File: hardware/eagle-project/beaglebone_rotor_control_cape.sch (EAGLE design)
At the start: 21 parts, among them IC1 TLC2264CDU, IC2 TLV5616, IC3 MAX3232ESE, Q1 SQ2348ES-T1-GE3, Q2 SQ2348ES-T1-GE3, X1 BEAGLEBONE_OUTLINE

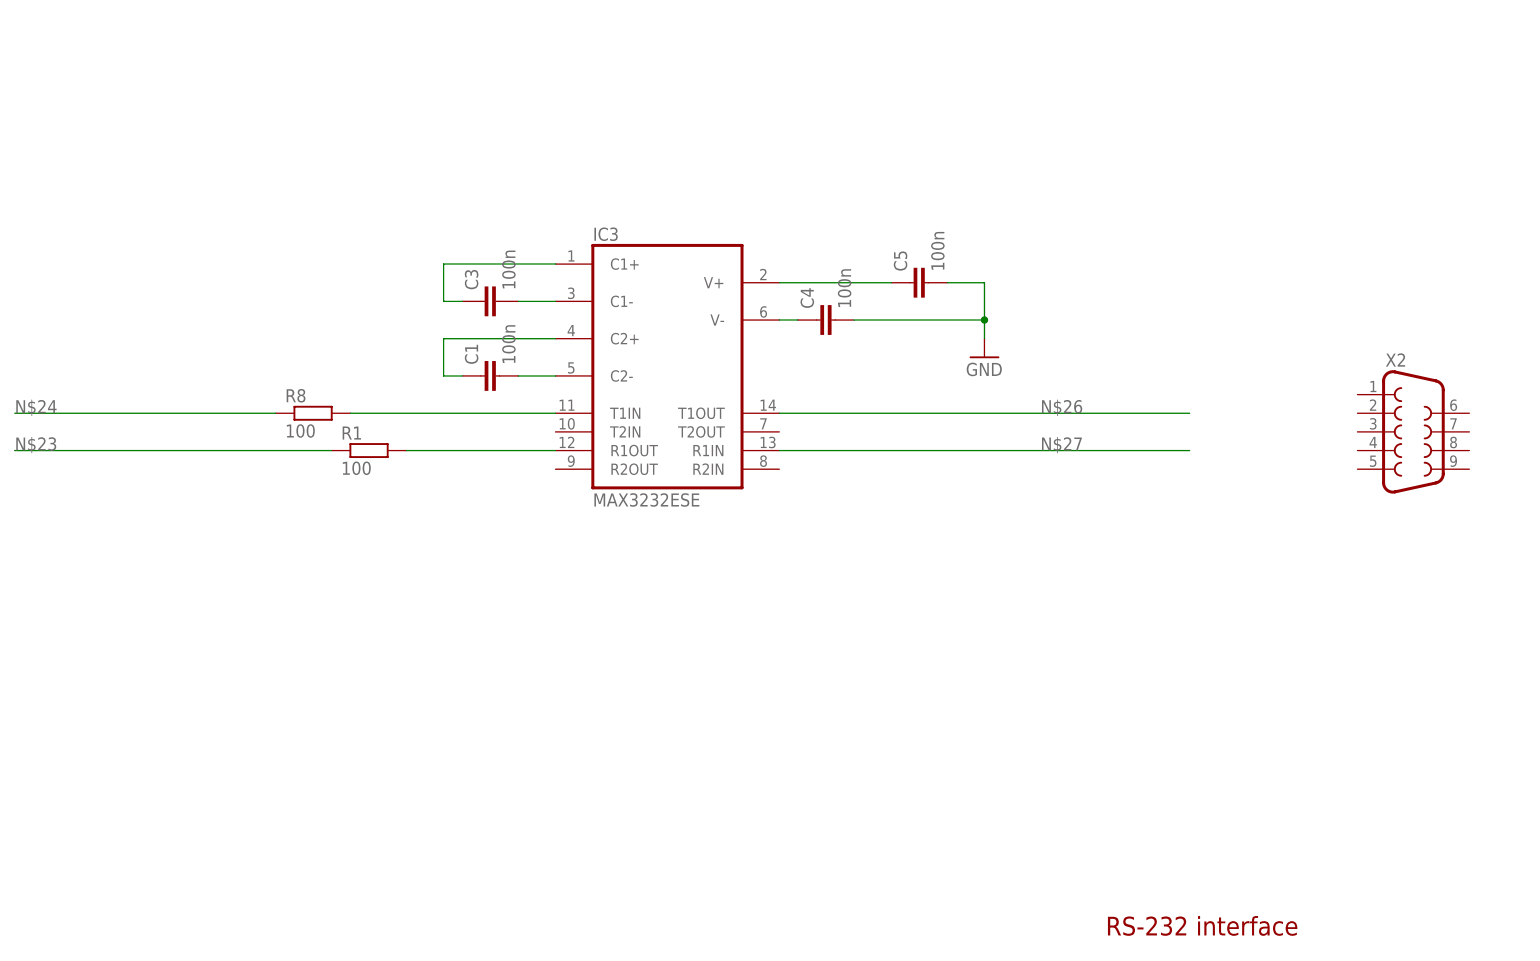
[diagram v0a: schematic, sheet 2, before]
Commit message: Eagle project update * RS232 rcv/drv layout done * AMP Press-Fit connector library created
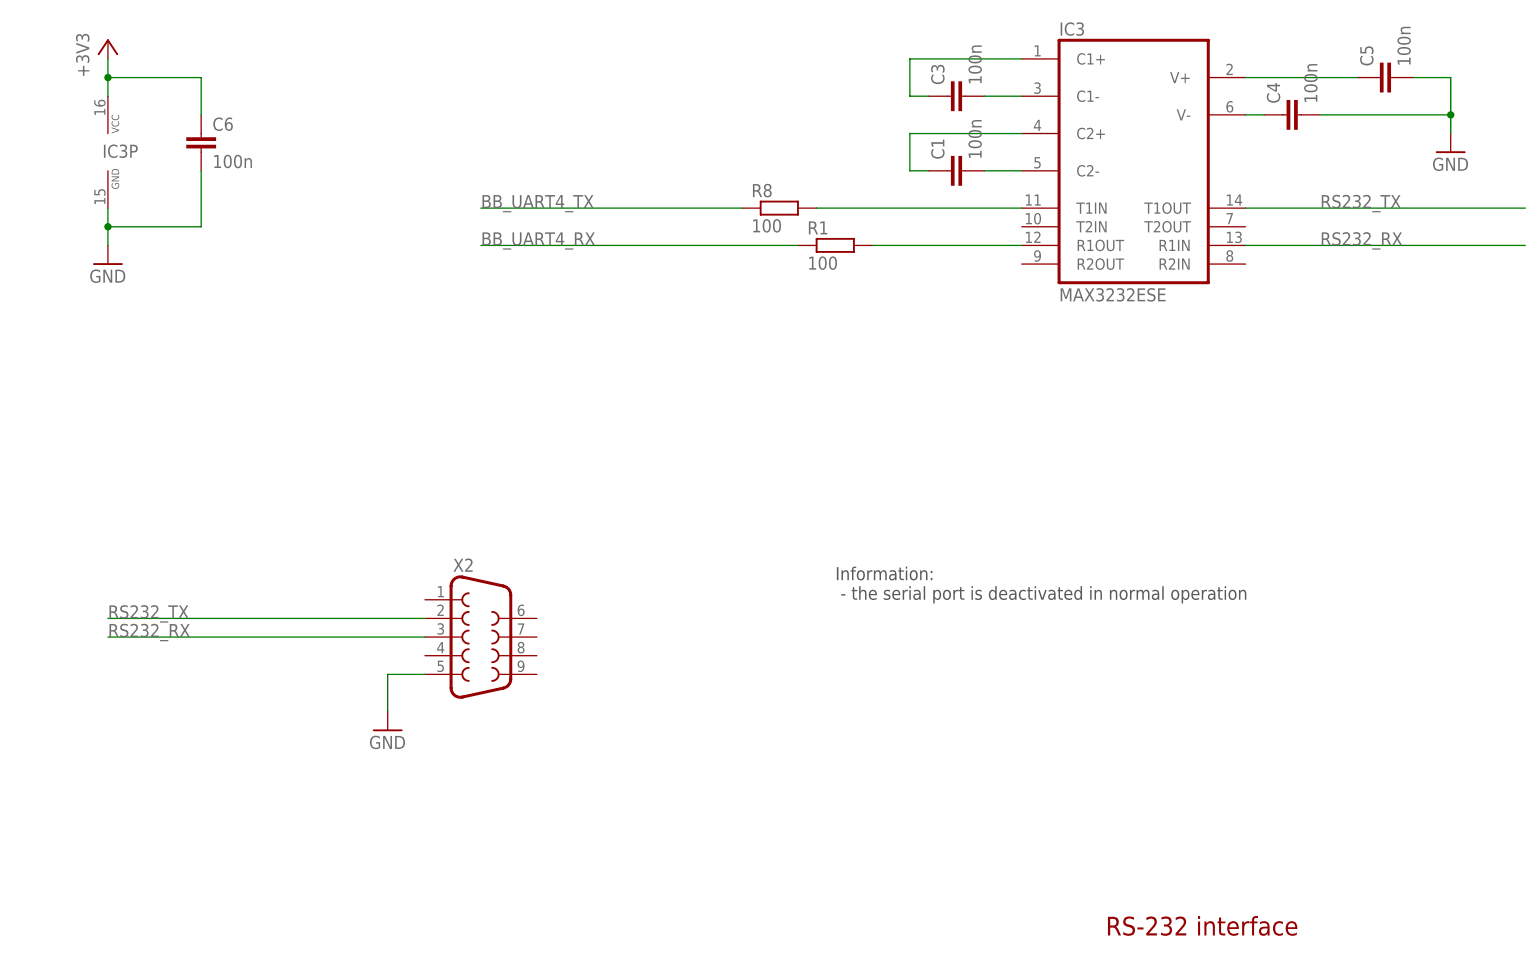
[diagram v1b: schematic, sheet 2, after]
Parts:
- removed R9: 15k, rcl:R-EU_R0805
- added C6: 100n, rcl:C-EUC0603
- added D1: BAS40-04, diode:BAS40-04
- added D2: 5V1, diode:ZENER-DIODESOT23
- added R10: 10k, rcl:R-EU_R0805
- R4: value (none) -> 10k
- R5: value (none) -> 5k6
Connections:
- removed net N$23: R1.1
- removed net N$24: R8.1
- removed net N$26: IC3G$1.T1OUT
- removed net N$27: IC3G$1.R1IN
- new net +3V3: C6.1, IC3P.VCC, X1.VDD_3V3EXP@1, X1.VDD_3V3EXP@2
- new net BB_UART4_RX: R1.1, X1.UART4_RXD
- new net BB_UART4_TX: R8.1, X1.UART4_TXD
- new net N$28: R10.2
- new net RS232_RX: IC3G$1.R1IN, X2.3
- new net RS232_TX: IC3G$1.T1OUT, X2.2
- net +5V: now also D1.C2, X1.VDD_5V@1, X1.VDD_5V@2
- net GND: now also C6.2, D1.A1, D2.A, IC3P.GND, X2.5; no longer R9.1
- net N$12: now also D1.C1A2, D2.C, R10.1; no longer R9.2
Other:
- note added: "Information: - the serial port is deactivated in normal operation"
- note removed: "todo überspannungsschutz"
- moved on the sheet: C1, C2, C3, C4, C5, IC1B, IC3, R1, R4, R5, R8, X2

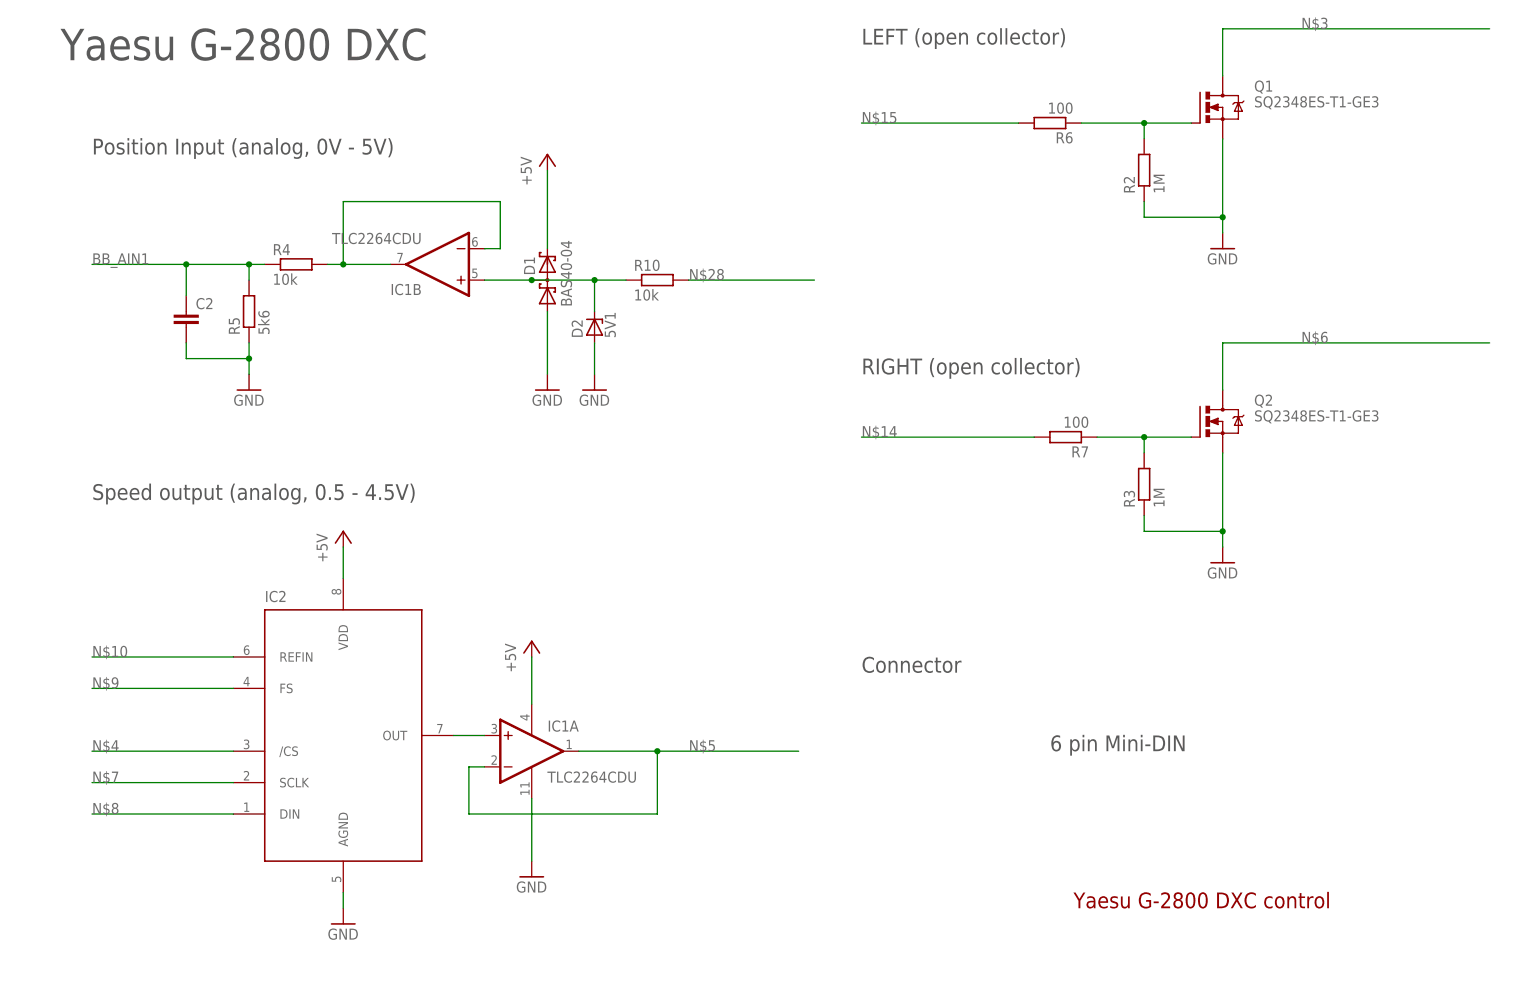
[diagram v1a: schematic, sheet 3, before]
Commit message: Updated available components list
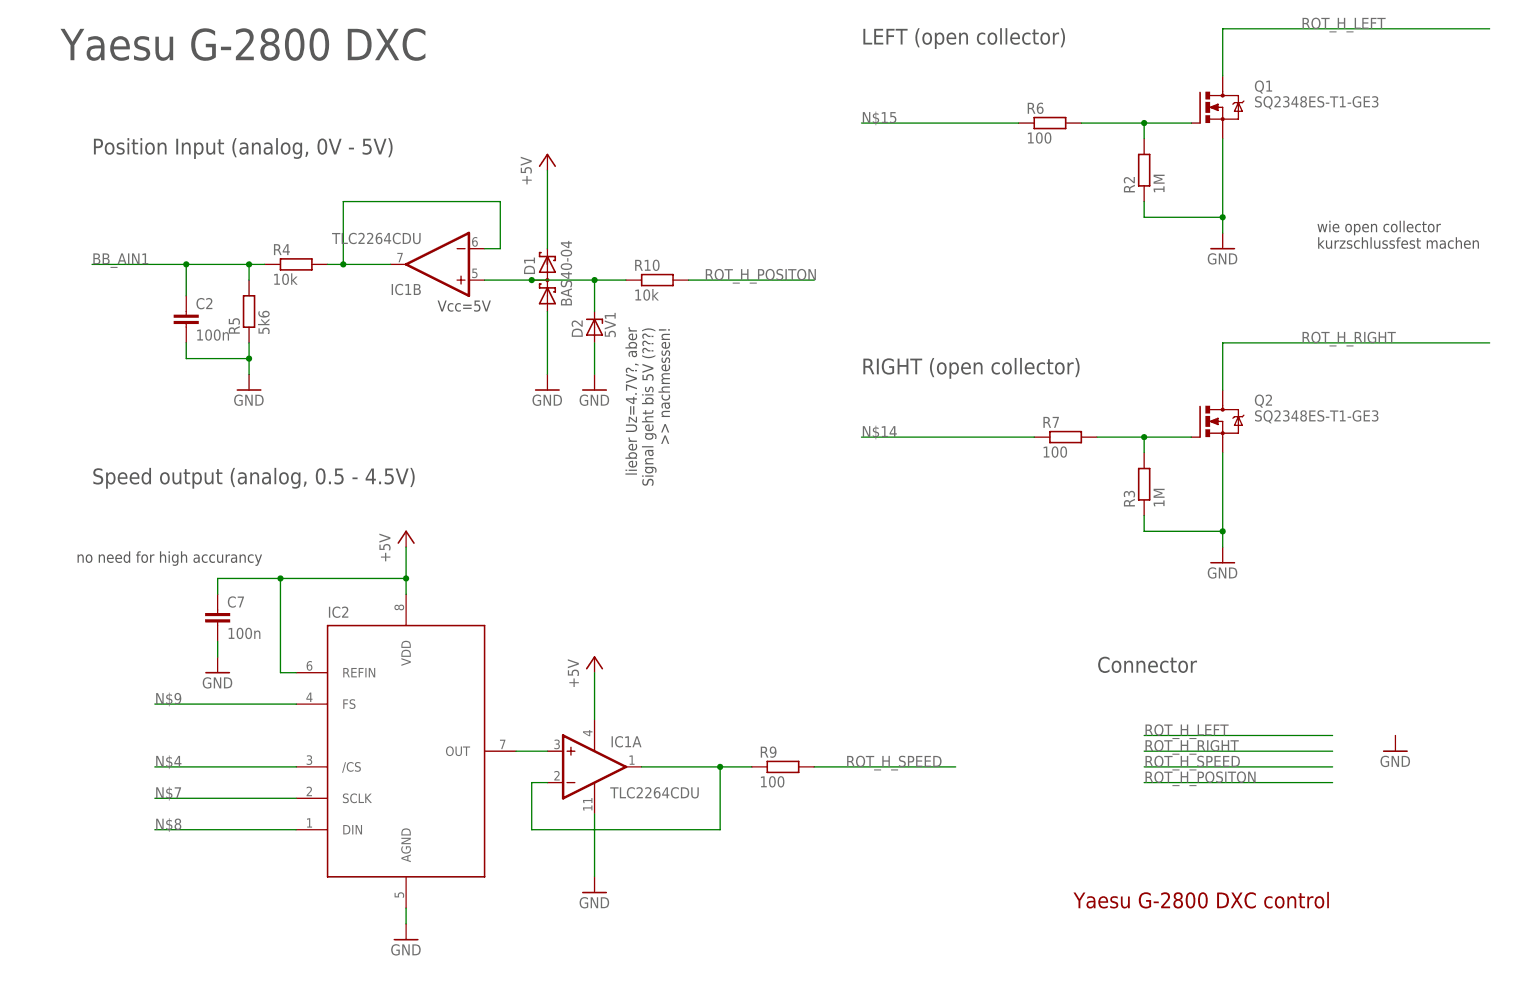
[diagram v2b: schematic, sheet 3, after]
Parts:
- added C7: 100n, rcl:C-EUC0603
- added R9: 100, rcl:R-EU_R0805
- C2: value (none) -> 100n
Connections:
- net N$28 renamed ROT_H_POSITON
- net N$3 renamed ROT_H_LEFT
- net N$6 renamed ROT_H_RIGHT
- removed net N$10: IC2.REFIN
- new net ROT_H_SPEED: R9.2
- net +5V: now also C7.1, IC2.REFIN
- net GND: now also C7.2
- net N$11: now also R7.2; no longer R7.1
- net N$13: now also R6.2; no longer R6.1
- net N$14: now also R7.1; no longer R7.2
- net N$15: now also R6.1; no longer R6.2
- net N$5: now also R9.1
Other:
- note added: "Vcc=5V"
- note added: "lieber Uz=4.7V?, aber Signal geht bis 5V (???) >> nachmessen!"
- note added: "no need for high accurancy"
- note added: "wie open collector kurzschlussfest machen"
- note removed: "6 pin Mini-DIN"
- moved on the sheet: IC1A, IC2, R6, R7

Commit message: New comments/thoughts in EAGLE schematics
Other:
- note added: "no need for high accurancy, maybe read this voltage for reference with ADC?"
- note removed: "no need for high accurancy"
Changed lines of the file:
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@@
 <grid distance="0.1" unitdist="inch" unit="inch" style="lines" multiple="1" display="no" altdistance="0.01" altunitdist="inch" altunit="inch"/>
 <layers>
-<layer number="1" name="Top" color="4" fill="1" visible="yes" active="no"/>
-<layer number="2" name="Route2" color="1" fill="3" visible="yes" active="no"/>
-<layer number="3" name="Route3" color="4" fill="3" visible="yes" active="no"/>
-<layer number="4" name="Route4" color="1" fill="4" visible="yes" active="no"/>
-<layer number="5" name="Route5" color="4" fill="4" visible="yes" active="no"/>
-<layer number="6" name="Route6" color="1" fill="8" visible="yes" active="no"/>
-<layer number="7" name="Route7" color="4" fill="8" visible="yes" active="no"/>
-<layer number="8" name="Route8" color="1" fill="2" visible="yes" active="no"/>
-<layer number="9" name="Route9" color="4" fill="2" visible="yes" active="no"/>
-<layer number="10" name="Route10" color="1" fill="7" visible="yes" active="no"/>
-<layer number="11" name="Route11" color="4" fill="7" visible="yes" active="no"/>
-<layer number="12" name="Route12" color="1" fill="5" visible="yes" active="no"/>
-<layer number="13" name="Route13" color="4" fill="5" visible="yes" active="no"/>
-<layer number="14" name="Route14" color="1" fill="6" visible="yes" active="no"/>
-<layer number="15" name="Route15" color="4" fill="6" visible="yes" active="no"/>
-<layer number="16" name="Bottom" color="1" fill="1" visible="yes" active="no"/>
-<layer number="17" name="Pads" color="2" fill="1" visible="yes" active="no"/>
-<layer number="18" name="Vias" color="2" fill="1" visible="yes" active="no"/>
-<layer number="19" name="Unrouted" color="6" fill="1" visible="yes" active="no"/>
-<layer number="20" name="Dimension" color="15" fill="1" visible="yes" active="no"/>
-<layer number="21" name="tPlace" color="7" fill="1" visible="yes" active="no"/>
-<layer number="22" name="bPlace" color="7" fill="1" visible="yes" active="no"/>
-<layer number="23" name="tOrigins" color="15" fill="1" visible="yes" active="no"/>
-<layer number="24" name="bOrigins" color="15" fill="1" visible="yes" active="no"/>
-<layer number="25" name="tNames" color="7" fill="1" visible="yes" active="no"/>
-<layer number="26" name="bNames" color="7" fill="1" visible="yes" active="no"/>
-<layer number="27" name="tValues" color="7" fill="1" visible="yes" active="no"/>
-<layer number="28" name="bValues" color="7" fill="1" visible="yes" active="no"/>
+<layer number="1" name="Top" color="4" fill="1" visible="no" active="no"/>
+<layer number="2" name="Route2" color="1" fill="3" visible="no" active="no"/>
+<layer number="3" name="Route3" color="4" fill="3" visible="no" active="no"/>
+<layer number="4" name="Route4" color="1" fill="4" visible="no" active="no"/>
+<layer number="5" name="Route5" color="4" fill="4" visible="no" active="no"/>
+<layer number="6" name="Route6" color="1" fill="8" visible="no" active="no"/>
+<layer number="7" name="Route7" color="4" fill="8" visible="no" active="no"/>
+<layer number="8" name="Route8" color="1" fill="2" visible="no" active="no"/>
+<layer number="9" name="Route9" color="4" fill="2" visible="no" active="no"/>
+<layer number="10" name="Route10" color="1" fill="7" visible="no" active="no"/>
+<layer number="11" name="Route11" color="4" fill="7" visible="no" active="no"/>
+<layer number="12" name="Route12" color="1" fill="5" visible="no" active="no"/>
+<layer number="13" name="Route13" color="4" fill="5" visible="no" active="no"/>
+<layer number="14" name="Route14" color="1" fill="6" visible="no" active="no"/>
+<layer number="15" name="Route15" color="4" fill="6" visible="no" active="no"/>
+<layer number="16" name="Bottom" color="1" fill="1" visible="no" active="no"/>
+<layer number="17" name="Pads" color="2" fill="1" visible="no" active="no"/>
+<layer number="18" name="Vias" color="2" fill="1" visible="no" active="no"/>
+<layer number="19" name="Unrouted" color="6" fill="1" visible="no" active="no"/>
+<layer number="20" name="Dimension" color="15" fill="1" visible="no" active="no"/>
+<layer number="21" name="tPlace" color="7" fill="1" visible="no" active="no"/>
+<layer number="22" name="bPlace" color="7" fill="1" visible="no" active="no"/>
+<layer number="23" name="tOrigins" color="15" fill="1" visible="no" active="no"/>
+<layer number="24" name="bOrigins" color="15" fill="1" visible="no" active="no"/>
+<layer number="25" name="tNames" color="7" fill="1" visible="no" active="no"/>
+<layer number="26" name="bNames" color="7" fill="1" visible="no" active="no"/>
+<layer number="27" name="tValues" color="7" fill="1" visible="no" active="no"/>
+<layer number="28" name="bValues" color="7" fill="1" visible="no" active="no"/>
 <layer number="29" name="tStop" color="7" fill="3" visible="no" active="no"/>
 <layer number="30" name="bStop" color="7" fill="6" visible="no" active="no"/>
@@
 <layer number="35" name="tGlue" color="7" fill="4" visible="no" active="no"/>
 <layer number="36" name="bGlue" color="7" fill="5" visible="no" active="no"/>
-<layer number="37" name="tTest" color="7" fill="1" visible="yes" active="no"/>
-<layer number="38" name="bTest" color="7" fill="1" visible="yes" active="no"/>
+<layer number="37" name="tTest" color="7" fill="1" visible="no" active="no"/>
+<layer number="38" name="bTest" color="7" fill="1" visible="no" active="no"/>
 <layer number="39" name="tKeepout" color="4" fill="11" visible="no" active="no"/>
 <layer number="40" name="bKeepout" color="1" fill="11" visible="no" active="no"/>
@@
 <layer number="44" name="Drills" color="7" fill="1" visible="no" active="no"/>
 <layer number="45" name="Holes" color="7" fill="1" visible="no" active="no"/>
-<layer number="46" name="Milling" color="3" fill="1" visible="yes" active="no"/>
-<layer number="47" name="Measures" color="7" fill="1" visible="yes" active="no"/>
-<layer number="48" name="Document" color="7" fill="1" visible="yes" active="no"/>
-<layer number="49" name="Reference" color="7" fill="1" visible="yes" active="no"/>
-<layer number="50" name="dxf" color="7" fill="1" visible="yes" active="no"/>
-<layer number="51" name="tDocu" color="7" fill="1" visible="yes" active="no"/>
-<layer number="52" name="bDocu" color="7" fill="1" visible="yes" active="no"/>
-<layer number="53" name="tGND_GNDA" color="7" fill="9" visible="yes" active="no"/>
-<layer number="54" name="bGND_GNDA" color="1" fill="9" visible="yes" active="no"/>
-<layer number="56" name="wert" color="7" fill="1" visible="yes" active="no"/>
-<layer number="57" name="tCAD" color="7" fill="1" visible="yes" active="no"/>
+<layer number="46" name="Milling" color="3" fill="1" visible="no" active="no"/>
+<layer number="47" name="Measures" color="7" fill="1" visible="no" active="no"/>
+<layer number="48" name="Document" color="7" fill="1" visible="no" active="no"/>
+<layer number="49" name="Reference" color="7" fill="1" visible="no" active="no"/>
+<layer number="50" name="dxf" color="7" fill="1" visible="no" active="no"/>
+<layer number="51" name="tDocu" color="7" fill="1" visible="no" active="no"/>
+<layer number="52" name="bDocu" color="7" fill="1" visible="no" active="no"/>
+<layer number="53" name="tGND_GNDA" color="7" fill="9" visible="no" active="no"/>
+<layer number="54" name="bGND_GNDA" color="1" fill="9" visible="no" active="no"/>
+<layer number="56" name="wert" color="7" fill="1" visible="no" active="no"/>
+<layer number="57" name="tCAD" color="7" fill="1" visible="no" active="no"/>
 <layer number="91" name="Nets" color="2" fill="1" visible="yes" active="yes"/>
 <layer number="92" name="Busses" color="1" fill="1" visible="yes" active="yes"/>
@@
 &gt;&gt; nachmessen!</text>
 <text x="76.2" y="116.84" size="1.778" layer="97">Vcc=5V</text>
-<text x="17.78" y="76.2" size="1.778" layer="97">no need for high accurancy</text>
+<text x="17.78" y="76.2" size="1.778" layer="97">no need for high accurancy,
+maybe read this voltage for
+reference with ADC?</text>
 <text x="218.44" y="127" size="1.778" layer="97">wie open collector
 kurzschlussfest machen</text>
